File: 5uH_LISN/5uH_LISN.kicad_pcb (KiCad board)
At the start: 2 copper layers, 100 x 50 mm, 37 parts, among them J1 BANANA_CONN, J2 BANANA_CONN, J3 BANANA_CONN, J4 BANANA_CONN

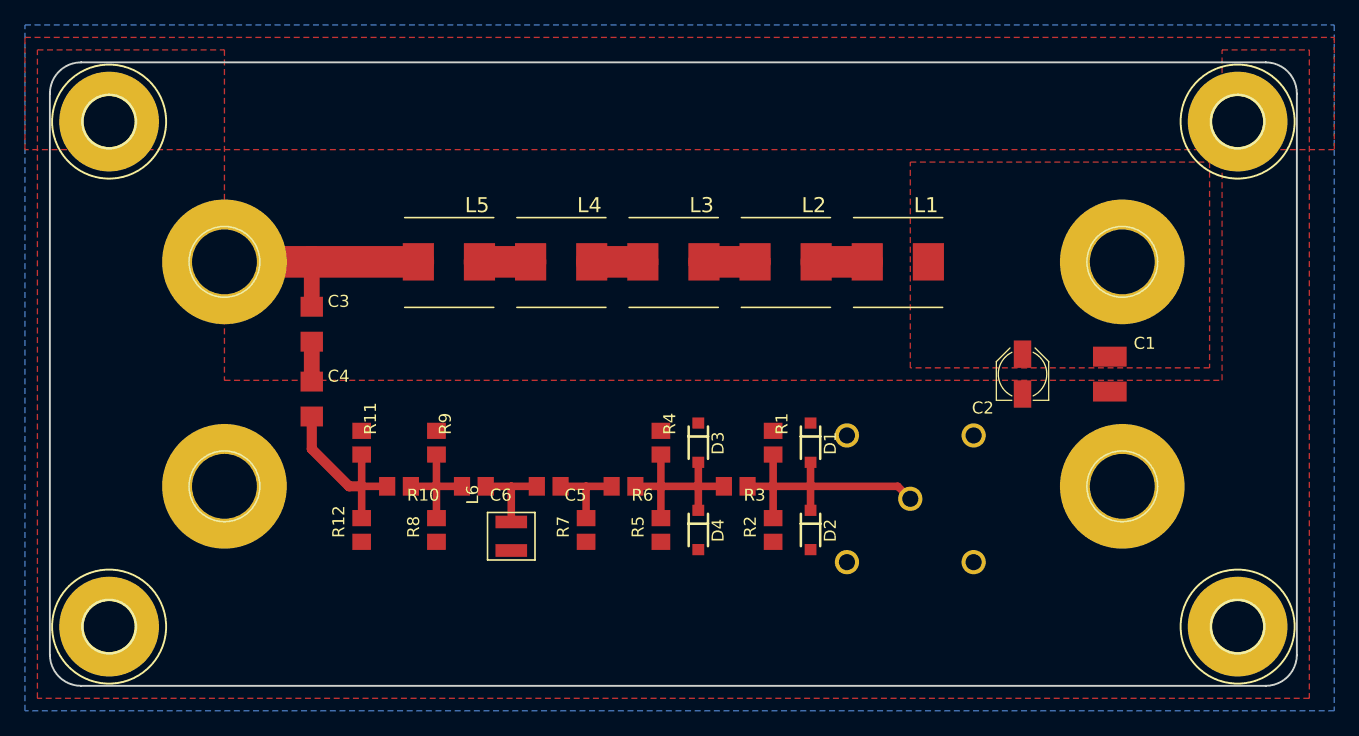
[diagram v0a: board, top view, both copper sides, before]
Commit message: Cleaned-up kicad layout.
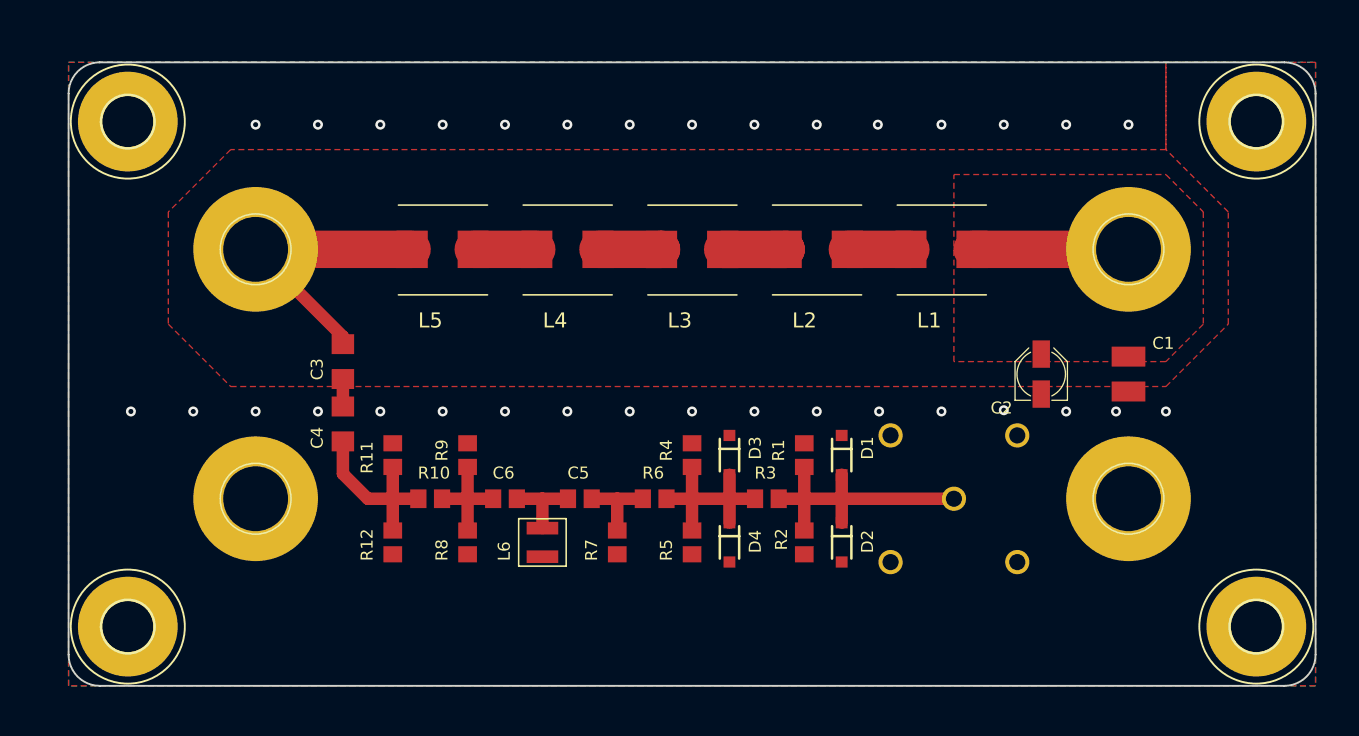
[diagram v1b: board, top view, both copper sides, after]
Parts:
- moved C3 3.90 mm to (122.0, 104.0)
- moved L1 3.64 mm to (170.0, 95.0)
- moved MEAS1 3.50 mm to (171.0, 115.0)
- moved C4 3.20 mm to (122.0, 109.0)
- moved J3 2.69 mm to (115.0, 95.0)
- moved L2 2.69 mm to (160.0, 95.0)
- moved J4 2.69 mm to (115.0, 115.0)
- moved R10 2.69 mm to (129.0, 115.0)
- moved R11 2.69 mm to (126.0, 111.5)
- moved R12 2.69 mm to (126.0, 118.5)
- moved C5 2.69 mm to (141.0, 115.0)
- moved C6 2.69 mm to (135.0, 115.0)
- moved D1 2.69 mm to (162.0, 111.5)
- moved D2 2.69 mm to (162.0, 118.5)
- moved D3 2.69 mm to (153.0, 111.5)
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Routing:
- net Net-(C1-Pad1): track 0.00 -> 12.6 mm
- net Net-(C3-Pad1): track 19.1 -> 23.0 mm
- net Net-(L3-Pad2): track 4.10 -> 5.10 mm
- net Net-(L2-Pad2): track 4.10 -> 5.10 mm
- net Net-(L4-Pad2): track 4.10 -> 5.10 mm
- net Net-(L1-Pad2): track 4.10 -> 5.10 mm
- net Net-(C3-Pad2): track 3.20 -> 2.20 mm
- net Net-(D1-PadA): track 22.4 -> 23.0 mm
- net GND: vias 0 -> 33
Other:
- board text added: "DESIGN BASED ON LINEAR TECHNOLOGY DC2130A"
- board text added: "MARTIN JÄGER (09/2016) WWW.LIBRE.SOLAR"
- board text added: "MAX 60V / 10A"
- board text removed: "Design based on Linear Technology DC2130A"
- board text removed: "Martin Jäger (09/2016) www.libre.solar"
- board text removed: "Maximum 60V / 10A"
